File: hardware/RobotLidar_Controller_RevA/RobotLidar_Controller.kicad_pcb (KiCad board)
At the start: 2 copper layers, 100 x 80 mm, 4 parts

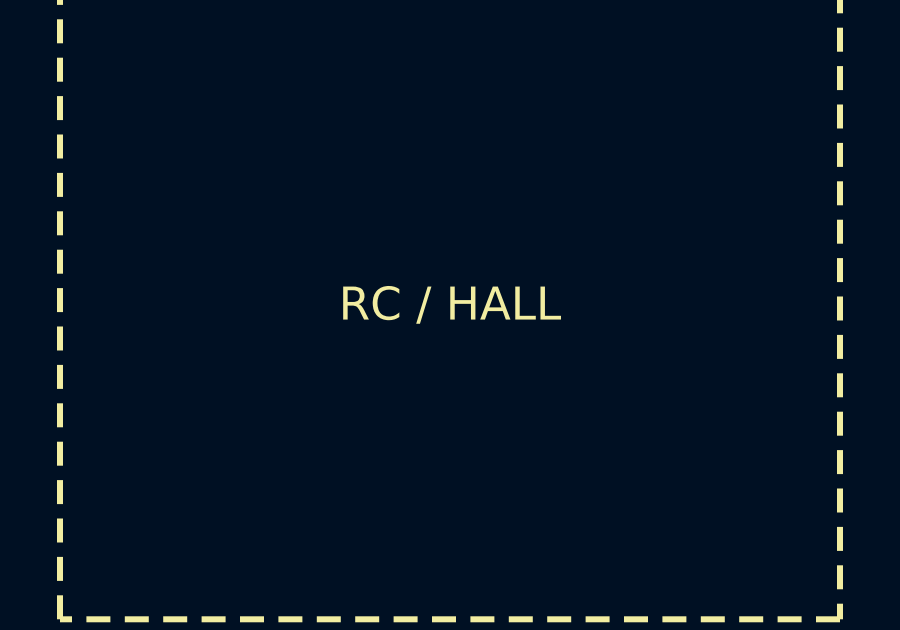
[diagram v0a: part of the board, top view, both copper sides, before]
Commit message: Label SBUS CH8 K155LA3 on Rev.A PCB
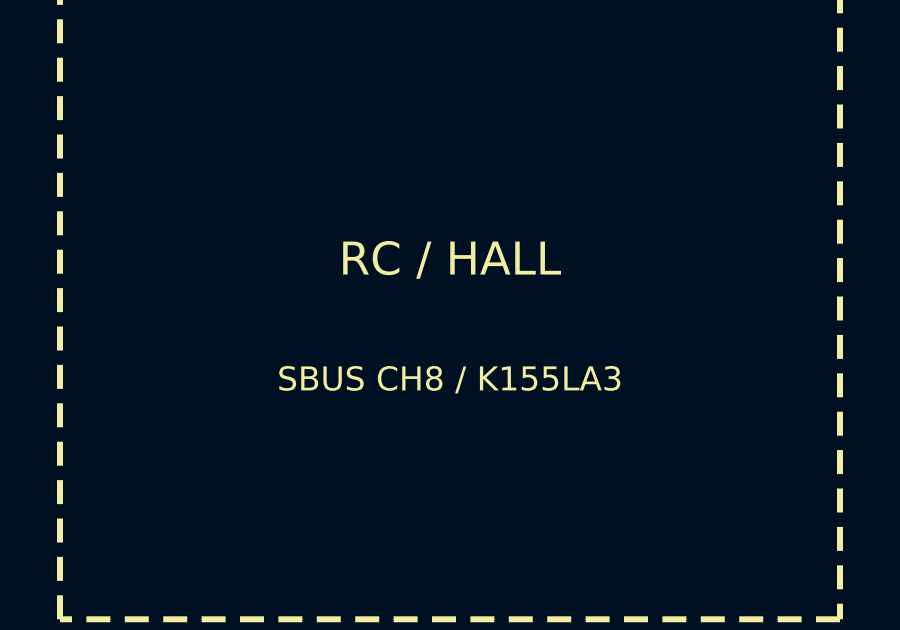
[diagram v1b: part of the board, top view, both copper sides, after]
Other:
- board text added: "SBUS CH8 / K155LA3"
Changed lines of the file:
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@@
   (gr_text "DRV8825 / M4" (at 100.5 42) (layer "F.SilkS") (effects (font (size 1.1 1.1))))
   (gr_rect (start 29 55) (end 55 76) (stroke (width 0.2) (type dash)) (fill none) (layer "F.SilkS"))
-  (gr_text "RC / HALL" (at 42 65.5) (layer "F.SilkS") (effects (font (size 1.1 1.1))))
+  (gr_text "RC / HALL" (at 42 64) (layer "F.SilkS") (effects (font (size 1.1 1.1))))
+  (gr_text "SBUS CH8 / K155LA3" (at 42 68) (layer "F.SilkS") (effects (font (size 0.8 0.8))))
   (gr_rect (start 60 55) (end 85 76) (stroke (width 0.2) (type dash)) (fill none) (layer "F.SilkS"))
   (gr_text "ANALOG / INA" (at 72.5 65.5) (layer "F.SilkS") (effects (font (size 1.1 1.1))))
